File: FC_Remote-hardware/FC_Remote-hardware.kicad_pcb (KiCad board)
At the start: 4 copper layers, 150 x 100 mm, 88 parts, among them J1 USB_C_Receptacle, J2 USB_C_Receptacle, Q3 MMBT2222A, Q4 MMBT2222A, SW1 SW_Push, SW3 SW_Push, SW4 SW_Push, SW5 SW_Push, SW6 SW_Push, SW8 SW_SPST, U1 COM-09032, U12 NRF24L01_Breakout, U2 COM-09032, U3 BQ25185DLHR, U4 ST7789_2IN_WS, U5 ATSAMD21G18A-AU, U6 ESP32-WROOM-32D, U7 NRF24L01_Breakout, U8 TPS63802DLAR, U9 CH340C

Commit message: added changes
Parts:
- removed BZ1: Buzzer, Buzzer_Beeper:Buzzer_12x9.5RM7.6
- removed F1, F2: Polyfuse, Fuse:Fuse_1206_3216Metric
- removed J2: USB_C_Receptacle, PCM_SparkFun-Connector:USB-C_16
- removed R22, R23: 100K, Resistor_SMD:R_0603_1608Metric
- removed R24: 100K, Resistor_SMD:R_0603_1608Metric_Pad0.98x0.95mm_HandSolder
- removed SW5: SW_Push, Button_Switch_SMD:SW_Push_1P1T_NO_CK_KSC7xxJ
- removed SW6: SW_Push, Button_Switch_SMD:SW_Push_1P1T_NO_CK_PTS125Sx85SMTR
- removed kibuzzard-6966E9EB: G***, kibuzzard-6966E9EB
- removed kibuzzard-6966E9F8: G***, kibuzzard-6966E9F8
- removed kibuzzard-6966EA20: G***, kibuzzard-6966EA20
- removed kibuzzard-6966F3E2: G***, kibuzzard-6966F3E2
- removed kibuzzard-6966F40D: G***, kibuzzard-6966F40D
- removed kibuzzard-6967171C: G***, kibuzzard-6967171C
- removed kibuzzard-6967172E: G***, kibuzzard-6967172E
- removed kibuzzard-696719AC: G***, kibuzzard-696719AC
- removed kibuzzard-696719EA: G***, kibuzzard-696719EA
- removed kibuzzard-69671E8B: G***, kibuzzard-69671E8B
- removed kibuzzard-69672012: G***, kibuzzard-69672012
- removed kibuzzard-69672043: G***, kibuzzard-69672043
- removed kibuzzard-69672213: G***, kibuzzard-69672213
- removed kibuzzard-696722D8: G***, kibuzzard-696722D8
- removed kibuzzard-69672723: G***, kibuzzard-69672723
- added C10: 1uF, Capacitor_SMD:C_0603_1608Metric, F.Cu at (225.9, 53.2)
- added C11: 10uF, Capacitor_SMD:C_0603_1608Metric, F.Cu at (225.9, 51.6)
- added C12: 1uF, Capacitor_SMD:C_0603_1608Metric, F.Cu at (155.3, 66.5)
- added C14: 0.1uF, Capacitor_SMD:C_0603_1608Metric, F.Cu at (133.3, 33.5)
- added C15: 0.1uF, Capacitor_SMD:C_0603_1608Metric, F.Cu at (209.3, 51.3)
- added C18: 0.1uF, Capacitor_SMD:C_0603_1608Metric, F.Cu at (212.9, 51.3)
- added C21: 22uF, PCM_SparkFun-Capacitor:C_0805_2012Metric, F.Cu at (215.0, -9.75)
- added C22: 22uF, PCM_SparkFun-Capacitor:C_0805_2012Metric, F.Cu at (93.8, -9.75)
- added D10: GREEN, LED_SMD:LED_0603_1608Metric_Pad1.05x0.95mm_HandSolder, F.Cu at (89.8, -5.25)
- added G***: LOGO, LOGO, F.Cu at (118.8, 1.92)
- added R27: 10K, Resistor_SMD:R_0603_1608Metric, F.Cu at (198.9, 52.1)
- added R28: 10K, Resistor_SMD:R_0603_1608Metric, F.Cu at (198.9, 49.0)
- added SW2: SW_SPST, SWITCHMTS101:mts101sw, F.Cu at (180.5, 44.0)
- added kibuzzard-69B816EF: G***, kibuzzard-69B816EF, F.Cu at (134.3, 52.7)
- added kibuzzard-69B81705: G***, kibuzzard-69B81705, F.Cu at (180.3, 52.7)
- added kibuzzard-69B818B8: G***, kibuzzard-69B818B8, F.Cu at (149.0, 40.4)
- added kibuzzard-69B818DE: G***, kibuzzard-69B818DE, F.Cu at (165.0, 40.4)
- added kibuzzard-69B825AF: G***, kibuzzard-69B825AF, F.Cu at (214.0, -3.75)
- added kibuzzard-69B825F7: G***, kibuzzard-69B825F7, F.Cu at (91.5, -3.50)
- added kibuzzard-69B8345C: G***, kibuzzard-69B8345C, F.Cu at (166.2, 62.9)
- added kibuzzard-69B83530: G***, kibuzzard-69B83530, F.Cu at (174.4, 63.0)
- added kibuzzard-69B8399F: G***, kibuzzard-69B8399F, F.Cu at (180.0, 82.4)
- added kibuzzard-69B842D9: G***, kibuzzard-69B842D9, F.Cu at (106.0, 61.4)
- added kibuzzard-69B842E6: G***, kibuzzard-69B842E6, F.Cu at (106.1, 68.4)
- added kibuzzard-69B84485: G***, kibuzzard-69B84485, F.Cu at (146.9, 68.1)
- added kibuzzard-69B84493: G***, kibuzzard-69B84493, F.Cu at (147.0, 74.3)
- C1, C2, C20, C3, C4, C5, C9, J1, L1, Q3, Q4, R10, R13, R14, R16, R17, R18, R4, R9, U3, U8, U9: moved to F.Cu
- C13: value 100uF -> 1uF; footprint Capacitor_THT:C_Radial_D6.3mm_H5.0mm_P2.50mm -> Capacitor_SMD:C_0603_1608Metric; moved to F.Cu
- C16: value 10uF -> 0.1uF
- C19: value 10uF -> 0.1uF; moved to F.Cu
- D7: value PESD0603-240 -> PMEG4020EJ; footprint PCM_SparkFun-Capacitor:C_0603_1608Metric -> Diode_SMD:D_SOD-323; moved to F.Cu
- D8: value PESD0603-240 -> GREEN; footprint PCM_SparkFun-Capacitor:C_0603_1608Metric -> LED_SMD:LED_0603_1608Metric_Pad1.05x0.95mm_HandSolder; moved to F.Cu
- R1: value DNP -> 10k; moved to F.Cu
- R11: value DNP -> 5K; footprint Resistor_SMD:R_0603_1608Metric -> Resistor_SMD:R_0603_1608Metric_Pad0.98x0.95mm_HandSolder; moved to F.Cu
- R12: value 18K -> 13K; moved to F.Cu
- R19: value 5.1k -> 10K; moved to F.Cu
- R2, R6: value 1K -> 5K; moved to F.Cu
- R20, R21: value R -> 470
- R3: value 500 -> 5K
- R5: value 5.1k -> 10k; moved to F.Cu
- R7: value 10K -> 5K; footprint Resistor_SMD:R_0603_1608Metric -> Resistor_SMD:R_0603_1608Metric_Pad0.98x0.95mm_HandSolder; moved to F.Cu
- R8: value 10k -> 10K; moved to F.Cu
- SW3: value SW_Push -> SW_SPST; footprint Button_Switch_SMD:SW_Push_1P1T_NO_CK_PTS125Sx85SMTR -> SWITCHMTS101:mts101sw
- U5: value ATSAMD21G18A-AU -> ESP32-WROVER-E-N16R8; footprint Package_DFN_QFN:QFN-48-1EP_7x7mm_P0.5mm_EP3.5x3.5mm_ThermalVias -> PCM_SparkFun-RF:ESP32-WROVER-E-IE; moved to F.Cu
- U6: value ESP32-WROOM-32D -> TPD2EUSB30; footprint RF_Module:ESP32-WROOM-32D -> Package_TO_SOT_SMD:Texas_DRT-3; moved to F.Cu
- moved R7 119.2 mm to (215.8, -5.50), turned to 180 degrees
- moved R3 105.7 mm to (107.6, 58.7)
- moved D5 105.4 mm to (103.3, 58.7), turned to 180 degrees
- moved C3 105.1 mm to (167.2, 76.9), turned to 180 degrees
- moved R15 104.9 mm to (107.4, 65.8)
- moved D3 104.7 mm to (103.1, 65.8)
- moved C19 104.3 mm to (226.0, 54.8)
- moved D8 100.8 mm to (212.1, -5.50)
- moved R5 91.9 mm to (221.5, 54.4)
- moved U6 89.2 mm to (160.3, 75.9), turned to 0 degrees
- moved C13 75.1 mm to (134.8, 33.5), turned to -90 degrees
- moved C1 73.8 mm to (193.5, 75.0)
- moved SW1 73.3 mm to (165.0, 44.7)
- moved R16 69.3 mm to (195.1, 79.0)
- moved R17 68.8 mm to (191.6, 79.0), turned to 180 degrees
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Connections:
- BT1 pad 1: VBAT -> GND
- BT1 pad 2: GND -> VBAT
- C13 pad 1: GND -> +3.3V
- C13 pad 2: VBAT -> GND
- C16 pad 1: GND -> DIR_JOY_X
- C16 pad 2: VBAT -> GND
- C17 pad 1: GND -> THROTTLE_JOY
- C17 pad 2: VBAT -> GND
- C19 pad 2: +5V -> +3.3V
- C20 pad 2: +5V -> +3.3V
- C3 pad 1: CHIP_PU -> +5V
- C9 pad 1: GND -> CHIP_PU
- C9 pad 2: Net-(U5-VDDCORE) -> GND
- D7 pad 2: GND -> Net-(D7-A)
- D8 pad 1: +5V -> GND
- D8 pad 2: GND -> Net-(D8-A)
- J1 pad VBUS: Net-(F2-Pad2) -> Net-(D7-A)
- R1 pad 1: +3.3V -> 0_ESP
- R1 pad 2: SAMD_SDA -> +3.3V
- R11 pad 2: SAMD_SCL -> Net-(D10-A)
- R19 pad 1: Net-(J2-CC1) -> FLIGHT_MODE_SW
- R5 pad 1: Net-(J2-CC2) -> +3.3V
- R5 pad 2: GND -> CHIP_PU
- R7 pad 1: GND -> +3.3V
- R7 pad 2: Net-(U3-~{CE}) -> Net-(D8-A)
- R8 pad 1: +3.3V -> AUTONOMY_SW
- R8 pad 2: CHIP_PU -> GND
- SW3 pad 1: 15_ESP -> AUTONOMY_SW
- SW3 pad 2: GND -> +3.3V
- U1 pad B1A: unconnected-(U1-SEL+-PadB1A) -> GND
- U1 pad H1: +3.3V -> GND
- U1 pad H2: I34_ESP -> GND
- U1 pad V2: I35_ESP -> THROTTLE_JOY
- U12 pad 3: A1_ESP -> CTRL_CE
- U12 pad 4: 21_ESP -> CTRL_CSN
- U12 pad 5: SCK_ESP -> NRF_SCK
- U12 pad 6: MOSI_ESP -> NRF_MOSI
- U12 pad 7: MISO_ESP -> NRF_MISO
- U12 pad 8: unconnected-(U12-IRQ-Pad8) -> CTRL_IRQ
- U2 pad B1A: unconnected-(U2-SEL+-PadB1A) -> DIR_JOY_BTN
- U2 pad H2: 14_ESP -> DIR_JOY_X
- U2 pad V2: A5_ESP -> DIR_JOY_Y
- U3 pad 4: Net-(U3-~{CE}) -> GND
- U4 pad 3: MOSI_ESP -> TFT_MOSI
- U4 pad 4: SCK_ESP -> TFT_SCK
- U4 pad 5: 17_ESP -> TFT_CS
- U4 pad 6: 27_ESP -> TFT_DC
- U4 pad 7: 32_ESP -> CHIP_PU
- U4 pad 8: 33_ESP -> TFT_BL
- U5 pad 1: unconnected-(U5-PA00-Pad1) -> GND
- U5 pad 10: unconnected-(U5-PA05-Pad10) -> TFT_BL
- U5 pad 11: unconnected-(U5-PA06-Pad11) -> TELM_IRQ
- U5 pad 12: unconnected-(U5-PA07-Pad12) -> NRF_MISO
- U5 pad 13: unconnected-(U5-PA08-Pad13) -> NRF_SCK
- U5 pad 14: unconnected-(U5-PA09-Pad14) -> CTRL_IRQ
- U5 pad 15: unconnected-(U5-PA10-Pad15) -> GND
- U5 pad 16: unconnected-(U5-PA11-Pad16) -> NRF_MOSI
- U5 pad 17: +3.3V -> unconnected-(U5-NC-Pad17)
- U5 pad 18: GND -> unconnected-(U5-NC-Pad18)
- U5 pad 19: SAMD_MOSI -> unconnected-(U5-NC-Pad19)
- U5 pad 2: unconnected-(U5-PA01-Pad2) -> +3.3V
- U5 pad 20: SAMD_SCK -> unconnected-(U5-NC-Pad20)
- U5 pad 21: SAMD_MISO -> unconnected-(U5-NC-Pad21)
- U5 pad 23: unconnected-(U5-PA14-Pad23) -> DIR_JOY_BTN
- U5 pad 24: unconnected-(U5-PA15-Pad24) -> CTRL_CSN
- U5 pad 25: unconnected-(U5-PA16-Pad25) -> 0_ESP
- U5 pad 26: unconnected-(U5-PA17-Pad26) -> TELM_CE
- U5 pad 29: unconnected-(U5-PA20-Pad29) -> TELM_CSN
- U5 pad 3: SAMD_A0 -> CHIP_PU
- U5 pad 30: unconnected-(U5-PA21-Pad30) -> TFT_SCK
- U5 pad 31: SAMD_SDA -> CTRL_CE
- U5 pad 32: SAMD_SCL -> unconnected-(U5-NC-Pad32)
- U5 pad 33: SAMD_D- -> TFT_CS
- U5 pad 34: SAMD_D+ -> RX_ESP
- U5 pad 35: GND -> TX_ESP
- U5 pad 36: +3.3V -> TFT_DC
- U5 pad 37: unconnected-(U5-PB22-Pad37) -> TFT_MOSI
- U5 pad 38: unconnected-(U5-PB23-Pad38) -> GND
- U5 pad 4: SAMD_A1 -> FLIGHT_MODE_SW
- U5 pad 5: GND -> AUTONOMY_SW
- U5 pad 6: +3.3V -> THROTTLE_JOY
- U5 pad 7: unconnected-(U5-PB08-Pad7) -> DIR_JOY_X
- U5 pad 8: unconnected-(U5-PB09-Pad8) -> DIR_JOY_Y
- U5 pad 9: SAMD_A3 -> BATT_ADC
- U6 pad 1: GND -> USB_D+_ESP
- U6 pad 2: +3.3V -> USB__D-_ESP
- U6 pad 3: CHIP_PU -> GND
- U7 pad 3: SAMD_A1 -> TELM_CE
- U7 pad 4: SAMD_A0 -> TELM_CSN
- U7 pad 5: SAMD_SCK -> NRF_SCK
- U7 pad 6: SAMD_MOSI -> NRF_MOSI
- U7 pad 7: SAMD_MISO -> NRF_MISO
- U7 pad 8: unconnected-(U7-IRQ-Pad8) -> TELM_IRQ
- U8 pad 5: Net-(U8-PG) -> unconnected-(U8-PG-Pad5)
- U9 pad 15: unconnected-(U9-R232-Pad15) -> GND
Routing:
- net GND: track 643.2 -> 186.8 mm, vias 13 -> 99
- net NRF_MISO: track 0.00 -> 228.1 mm, vias 0 -> 2
- net NRF_SCK: track 0.00 -> 225.4 mm, vias 0 -> 2
- net NRF_MOSI: track 0.00 -> 208.3 mm, vias 0 -> 2
- net CTRL_CSN: track 0.00 -> 185.1 mm, vias 0 -> 3
- net CTRL_CE: track 0.00 -> 173.4 mm, vias 0 -> 4
- net +3.3V: track 541.8 -> 707.0 mm, vias 4 -> 2
- net THROTTLE_JOY: track 0.00 -> 155.0 mm, vias 0 -> 1
- net CTRL_IRQ: track 0.00 -> 138.4 mm, vias 0 -> 2
- net TFT_DC: track 0.00 -> 137.6 mm, vias 0 -> 6
- net TFT_CS: track 0.00 -> 136.9 mm, vias 0 -> 5
- net 14_ESP: track 134.3 -> 0.00 mm, vias 1 -> 0
- net TFT_MOSI: track 0.00 -> 131.7 mm, vias 0 -> 5
- net TFT_SCK: track 0.00 -> 128.3 mm, vias 0 -> 5
- net SCK_ESP: track 124.7 -> 0.00 mm
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- added copper zone on F.Cu, net GND
- removed copper zone on B.Cu, net +3.3V
- removed copper zone on B.Cu, net +5V
- removed copper zone on In2.Cu, net GND
- removed copper zone on B.Cu, net VBAT
- removed copper zone on B.Cu, net VS
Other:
- outline, holes or cut-outs redrawn
- board text added: "+ -"

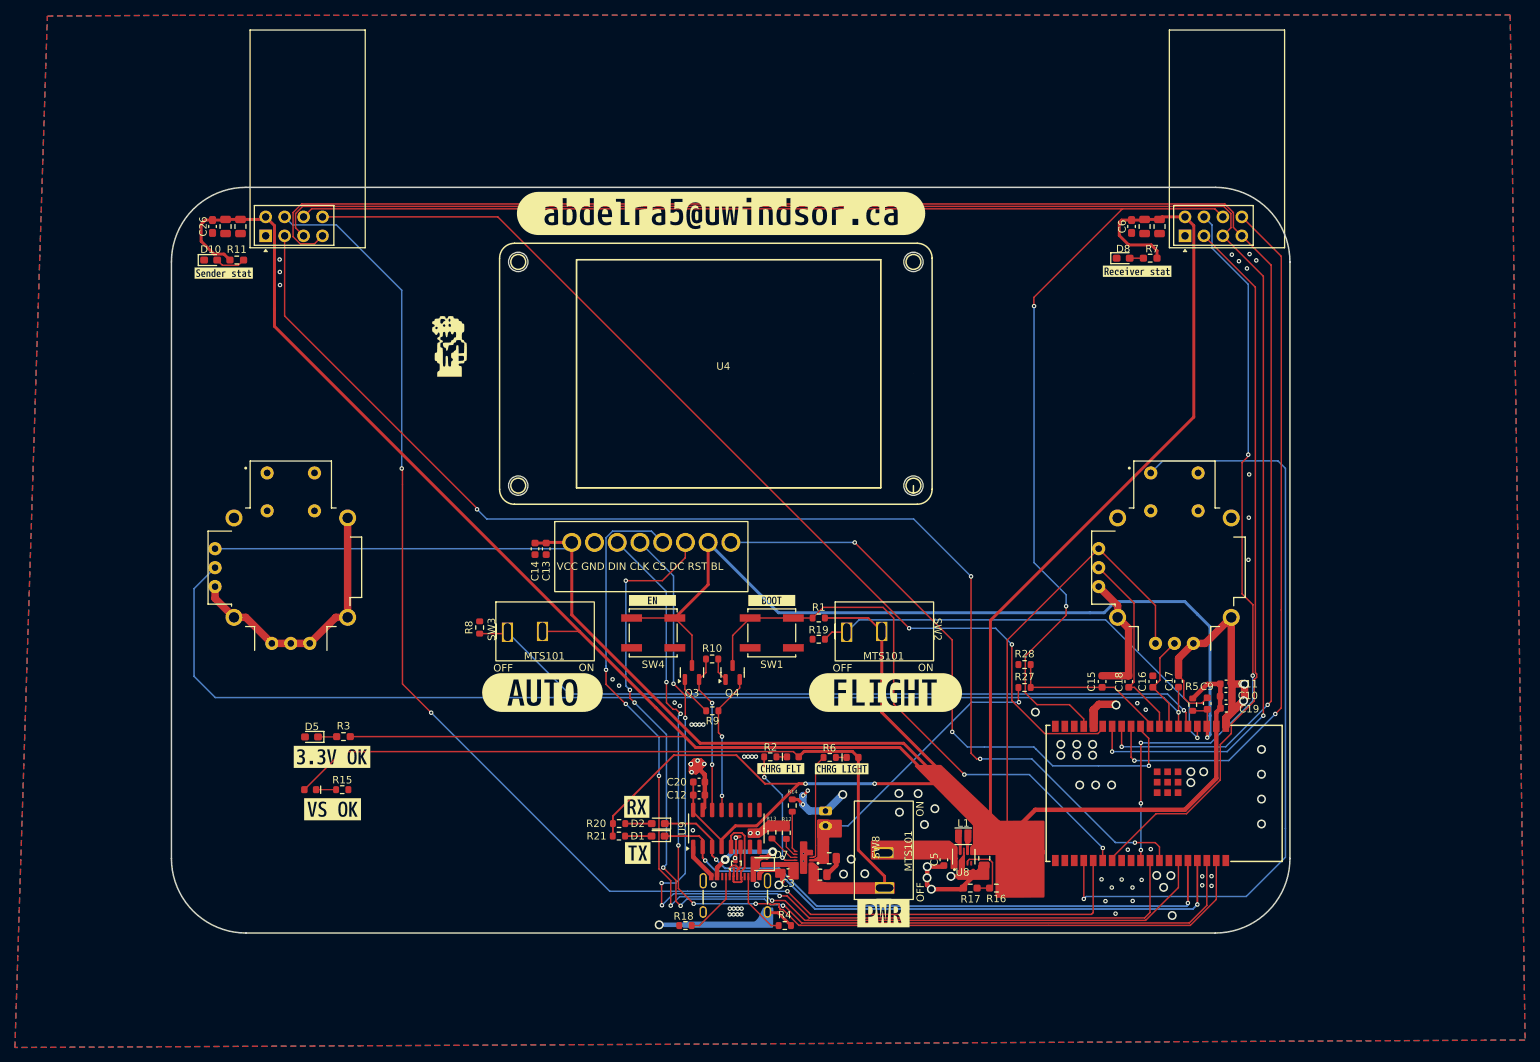
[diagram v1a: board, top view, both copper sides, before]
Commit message: added needed holes
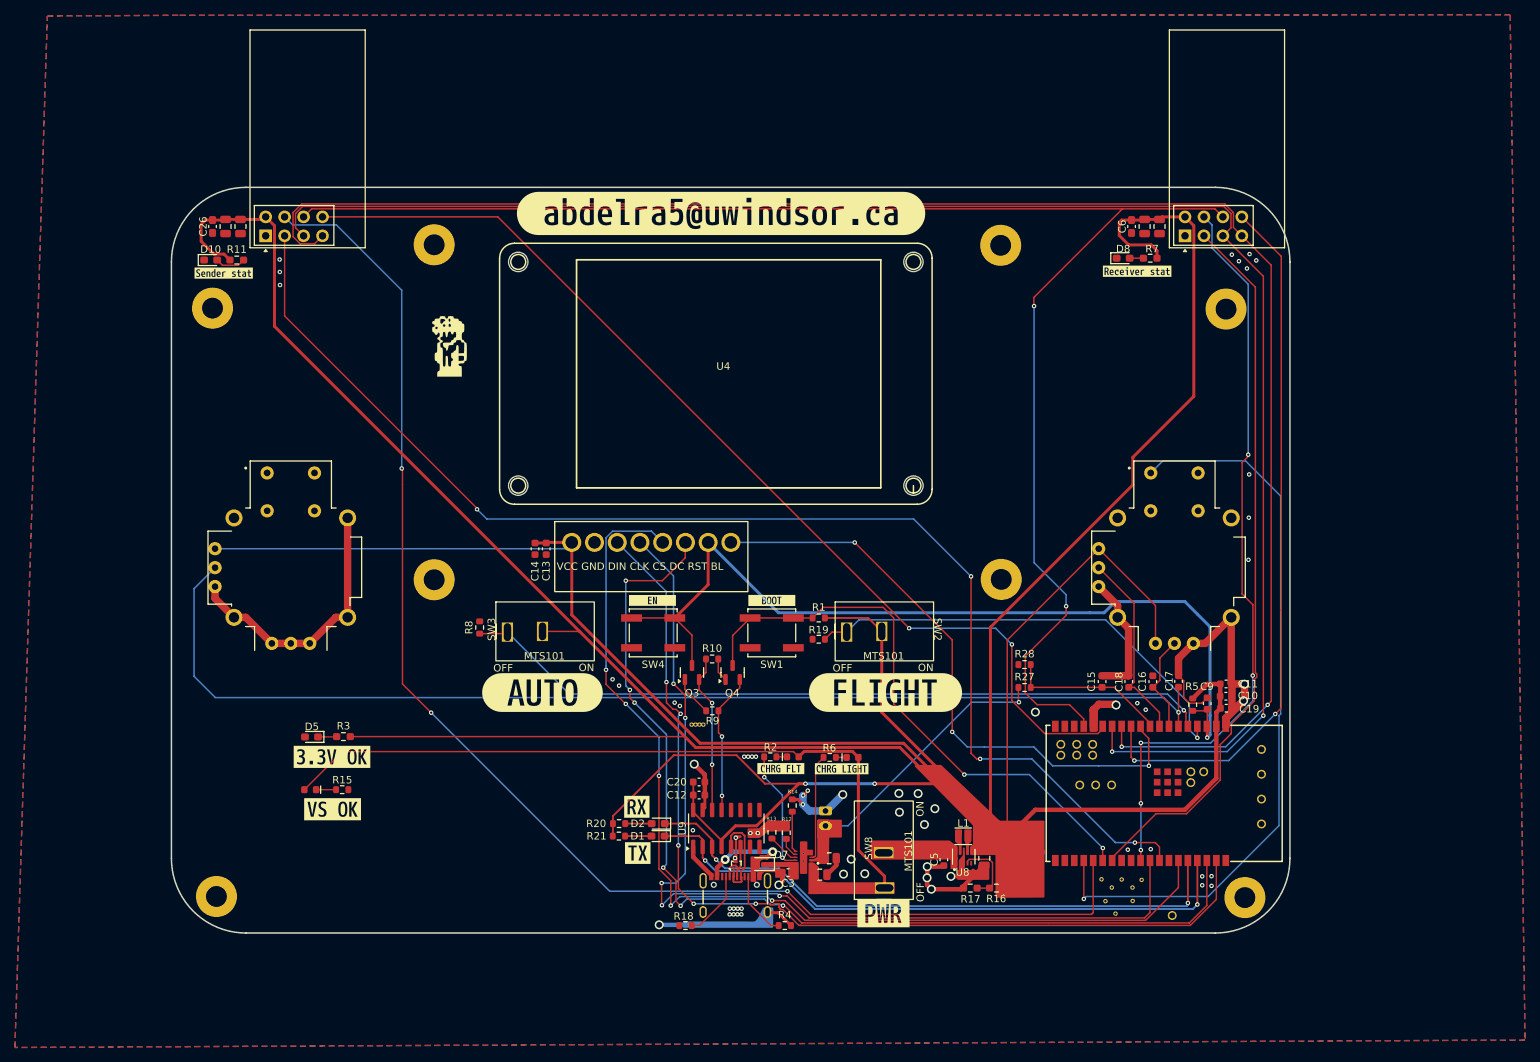
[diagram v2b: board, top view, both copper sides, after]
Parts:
- added ?: , , F.Cu at (221.2, 63.4)
- added ?: , , F.Cu at (154.8, 57.0)
- added ?: , , F.Cu at (213.4, 78.9)
- added ?: , , F.Cu at (119.7, 37.6)
- added ?: , , F.Cu at (209.2, 77.8)
- added ?: , , F.Cu at (230.7, 70.4)
- added ?: , , F.Cu at (211.1, 82.4)
- added ?: , , F.Cu at (228.5, 80.2)
- added ?: , , F.Cu at (230.7, 67.0)
- added ?: , , F.Cu at (222.9, 63.4)
- added ?: , , F.Cu at (119.7, -7.30)
- added ?: , , F.Cu at (208.4, 65.1)
- added ?: , , F.Cu at (221.2, 64.8)
- added ?: , , F.Cu at (205.9, 59.7)
- added ?: , , F.Cu at (230.7, 63.7)
- added ?: , , F.Cu at (208.0, 59.7)
- added ?: , , F.Cu at (155.8, 57.0)
- added ?: , , F.Cu at (208.0, 61.1)
- added ?: , , F.Cu at (90.5, 80.1)
- added ?: , , F.Cu at (230.7, 60.4)
- added ?: , , F.Cu at (210.6, 78.9)
- added ?: , , F.Cu at (90.0, 1.20)
- added ?: , , F.Cu at (203.8, 61.1)
- added ?: , , F.Cu at (195.8, 37.6)
- added ?: , , F.Cu at (214.6, 77.9)
- added ?: , , F.Cu at (195.7, -7.23)
- added ?: , , F.Cu at (205.9, 61.1)
- added ?: , , F.Cu at (210.6, 65.1)
- added ?: , , F.Cu at (213.4, 80.7)
- added ?: , , F.Cu at (203.8, 59.7)
- added ?: , , F.Cu at (209.8, 80.7)
- added ?: , , F.Cu at (155.3, 57.0)
- added ?: , , F.Cu at (218.7, 82.6)
- added ?: , , F.Cu at (211.9, 77.8)
- added ?: , , F.Cu at (225.9, 1.32)
- added ?: , , F.Cu at (154.3, 57.0)
- added ?: , , F.Cu at (206.3, 65.1)
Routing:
- net GND: track 186.8 -> 173.1 mm, vias 99 -> 63
- net DIR_JOY_BTN: track 105.8 -> 99.7 mm

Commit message: changed errors
new
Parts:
- removed the ? at (154.8, 57.0)
- removed the ? at (155.3, 57.0)
- moved kibuzzard-6967276B 0.55 mm to (158.3, -11.0)
- moved ? 0.43 mm to (90.5, 79.7)
- moved ? 0.15 mm to (228.5, 80.1)
- moved ? 0.12 mm to (225.9, 1.20)
- moved ? 0.10 mm to (155.9, 57.0)
- moved ? 0.07 mm to (195.7, 37.6)
- moved ? 0.05 mm to (119.7, 37.6)
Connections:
- J1 pad NC1: unconnected-(J1-NC-PadNC1) -> GND
- J1 pad NC2: unconnected-(J1-NC-PadNC2) -> GND
- J1 pad NC3: unconnected-(J1-NC-PadNC3) -> GND
- U3 pad 12: (no net) -> GND
- U3 pad 13: (no net) -> GND
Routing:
- net GND: track 173.1 -> 244.8 mm, vias 63 -> 78
- net Net-(U3-STAT2): track 14.3 -> 14.9 mm
